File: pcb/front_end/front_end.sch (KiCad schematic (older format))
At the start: 46 parts, among them J1 SMA, J10 SMA, J11 SMA, J12 SMA, J13 SMA, J14 SMA, J15 SMA, J16 SMA, J17 SMA, J18 SMA, J19 SMA, J2 SMA, J20 SMA, J21 SMA, J22 SMA, J23 SMA, J24 SMA, J25 SMA, J26 SMA, J27 SMA, J28 SMA, J29 SMA, J3 SMA, J30 SMA, J31 SMA, J32 SMA, J33 SMA, J4 SMA, J5 SMA, J6 SMA, J7 SMP, J8 SMP, J9 SMA

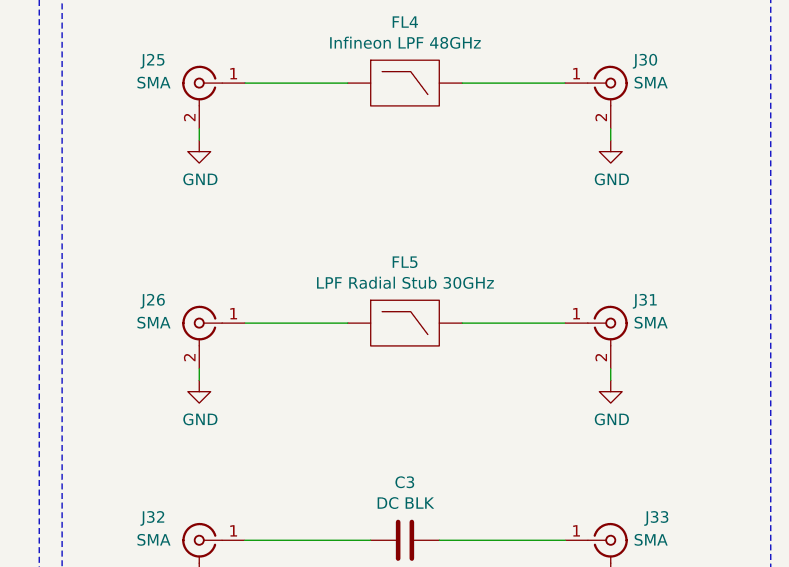
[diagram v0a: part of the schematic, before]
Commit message: Updated frontend layout with new LPF
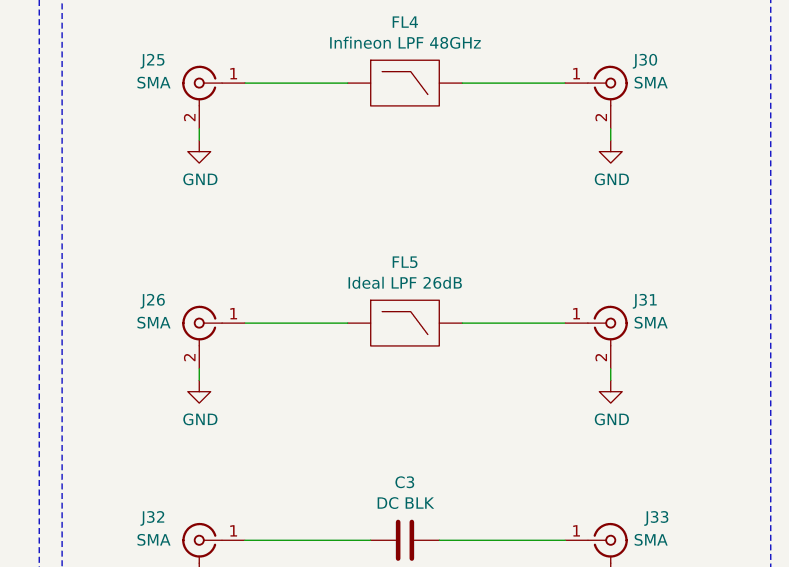
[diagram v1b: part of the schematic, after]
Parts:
- FL5: value LPF Radial Stub 30GHz -> Ideal LPF 26dB; footprint bloop:Radial_Stub_30GHz -> bloop:Ideal_LPF_26dB
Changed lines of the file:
@@
 EESchema Schematic File Version 4
 LIBS:front_end-cache
-EELAYER 30 0
+EELAYER 29 0
 EELAYER END
 $Descr B 17000 11000
@@
 P 13250 5550
 F 0 "FL5" H 13250 5815 50  0000 C CNN
-F 1 "LPF Radial Stub 30GHz" H 13250 5724 50  0000 C CNN
-F 2 "bloop:Radial_Stub_30GHz" H 13250 5300 50  0001 C CNN
+F 1 "Ideal LPF 26dB" H 13250 5724 50  0000 C CNN
+F 2 "bloop:Ideal_LPF_26dB" H 13250 5300 50  0001 C CNN
 F 3 "" H 12750 5800 50  0001 C CNN
 	1    13250 5550

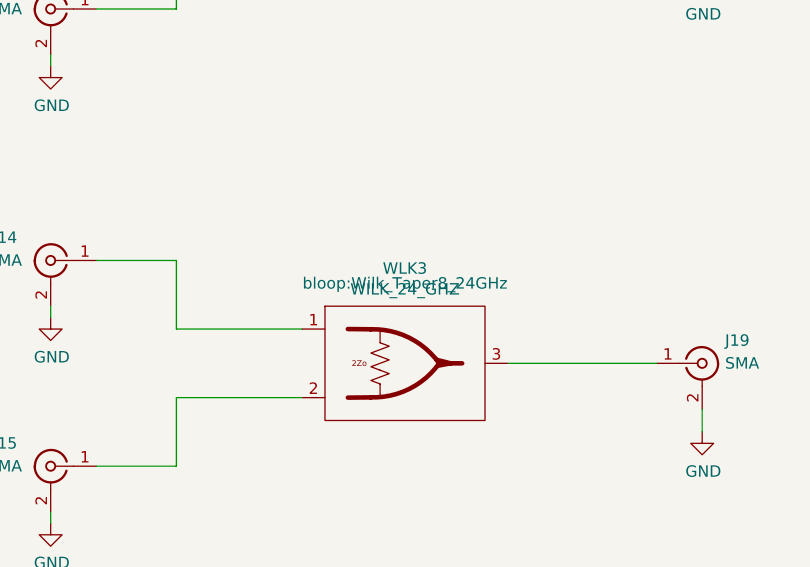
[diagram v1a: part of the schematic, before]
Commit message: Include modified AWR wilkinson design; need to correct chamfers and wilkinson line lengths
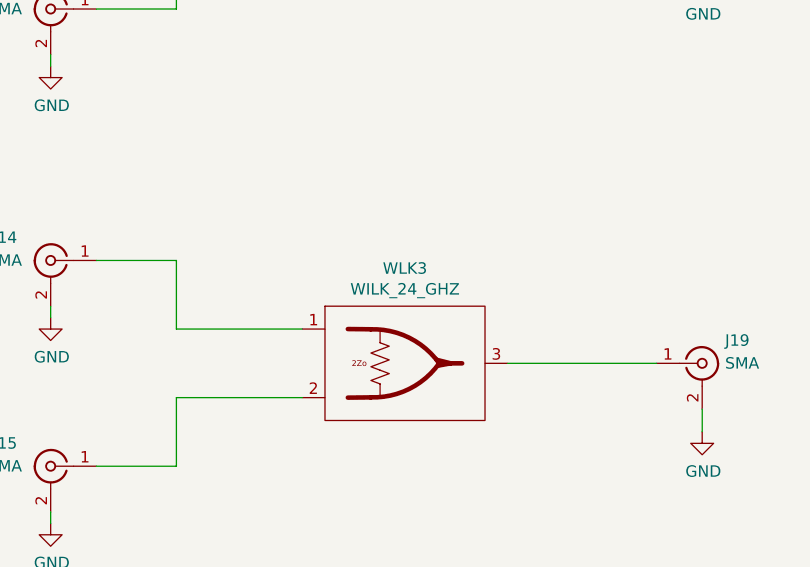
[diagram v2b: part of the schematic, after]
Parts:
- WLK1, WLK4: footprint bloop:Wilkinson_V1 -> bloop:Wilk_AWR_Mod
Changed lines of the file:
@@
 EESchema Schematic File Version 4
 LIBS:front_end-cache
-EELAYER 29 0
+EELAYER 30 0
 EELAYER END
 $Descr B 17000 11000
@@
 F 0 "WLK1" H 8150 2265 50  0000 C CNN
 F 1 "WILK_24_GHZ" H 8150 2174 50  0000 C CNN
-F 2 "bloop:Wilkinson_V1" H 8150 2200 50  0001 C CNN
+F 2 "bloop:Wilk_AWR_Mod" H 8150 2200 50  0001 C CNN
 F 3 "" H 8150 2200 50  0001 C CNN
 	1    8150 1850
@@
 F 0 "WLK3" H 9000 7115 50  0000 C CNN
 F 1 "WILK_24_GHZ" H 9000 7024 50  0000 C CNN
-F 2 "bloop:Wilk_Taper8_24GHz" H 9000 7050 50  0000 C CNN
+F 2 "bloop:Wilk_Taper8_24GHz" H 9000 7050 50  0001 C CNN
 F 3 "" H 9000 7050 50  0001 C CNN
 	1    9000 6700
@@
 F 0 "WLK4" H 9000 9115 50  0000 C CNN
 F 1 "WILK_24_GHZ" H 9000 9024 50  0000 C CNN
-F 2 "bloop:Wilkinson_V1" H 9000 9050 50  0001 C CNN
+F 2 "bloop:Wilk_AWR_Mod" H 9000 9050 50  0001 C CNN
 F 3 "" H 9000 9050 50  0001 C CNN
 	1    9000 8700

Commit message: Add bloop logo's; correct silkscreen; change to 0402 RF footprint; add wilkinson solder mask
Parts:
- C3: footprint Capacitor_SMD:C_0402_1005Metric -> bloop:C_0402_RF
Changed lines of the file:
@@
 	14150 6700 14150 6750
 $Comp
-L power:GND #PWR?
+L power:GND #PWR0102
 U 1 1 5D80B028
 P 14150 6750
-F 0 "#PWR?" H 14150 6500 50  0001 C CNN
+F 0 "#PWR0102" H 14150 6500 50  0001 C CNN
 F 1 "GND" H 14155 6577 50  0000 C CNN
 F 2 "" H 14150 6750 50  0001 C CNN
@@
 	13400 6500 13950 6500
 $Comp
-L power:GND #PWR?
+L power:GND #PWR0121
 U 1 1 5D80B02F
 P 12350 6750
-F 0 "#PWR?" H 12350 6500 50  0001 C CNN
+F 0 "#PWR0121" H 12350 6500 50  0001 C CNN
 F 1 "GND" H 12355 6577 50  0000 C CNN
 F 2 "" H 12350 6750 50  0001 C CNN
@@
 F 0 "C3" V 12998 6500 50  0000 C CNN
 F 1 "DC BLK" V 13089 6500 50  0000 C CNN
-F 2 "Capacitor_SMD:C_0402_1005Metric" H 13288 6350 50  0001 C CNN
+F 2 "bloop:C_0402_RF" H 13288 6350 50  0001 C CNN
 F 3 "~" H 13250 6500 50  0001 C CNN
 	1    13250 6500
